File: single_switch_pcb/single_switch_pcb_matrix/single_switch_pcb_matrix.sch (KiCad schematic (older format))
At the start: 50 parts

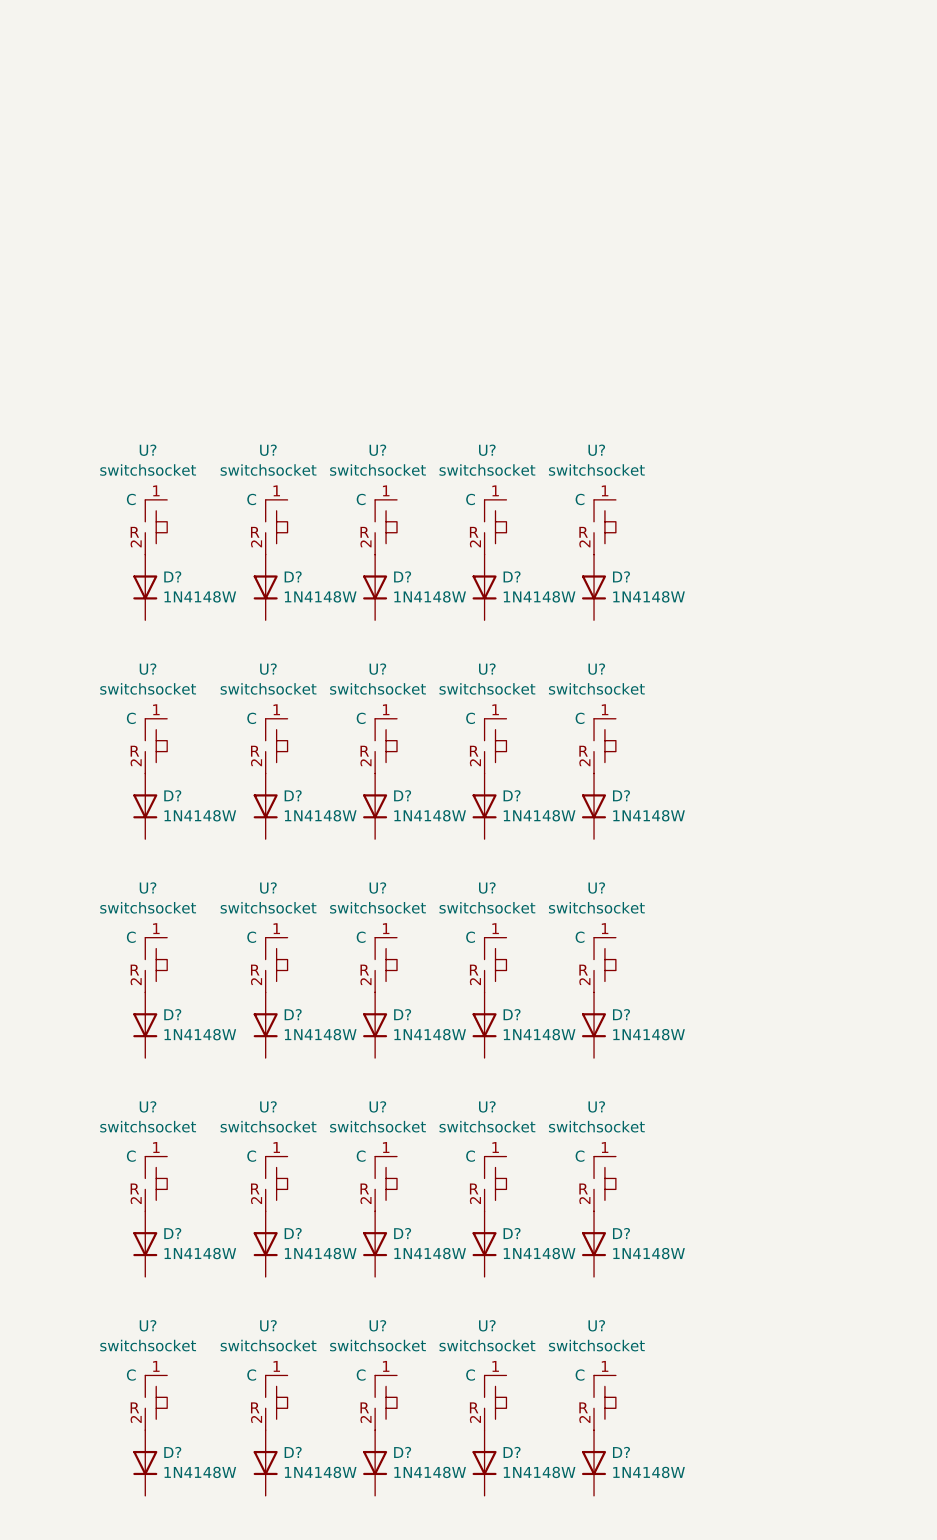
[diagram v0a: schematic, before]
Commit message: pcb matrix. done with column matrix. To do row matrix
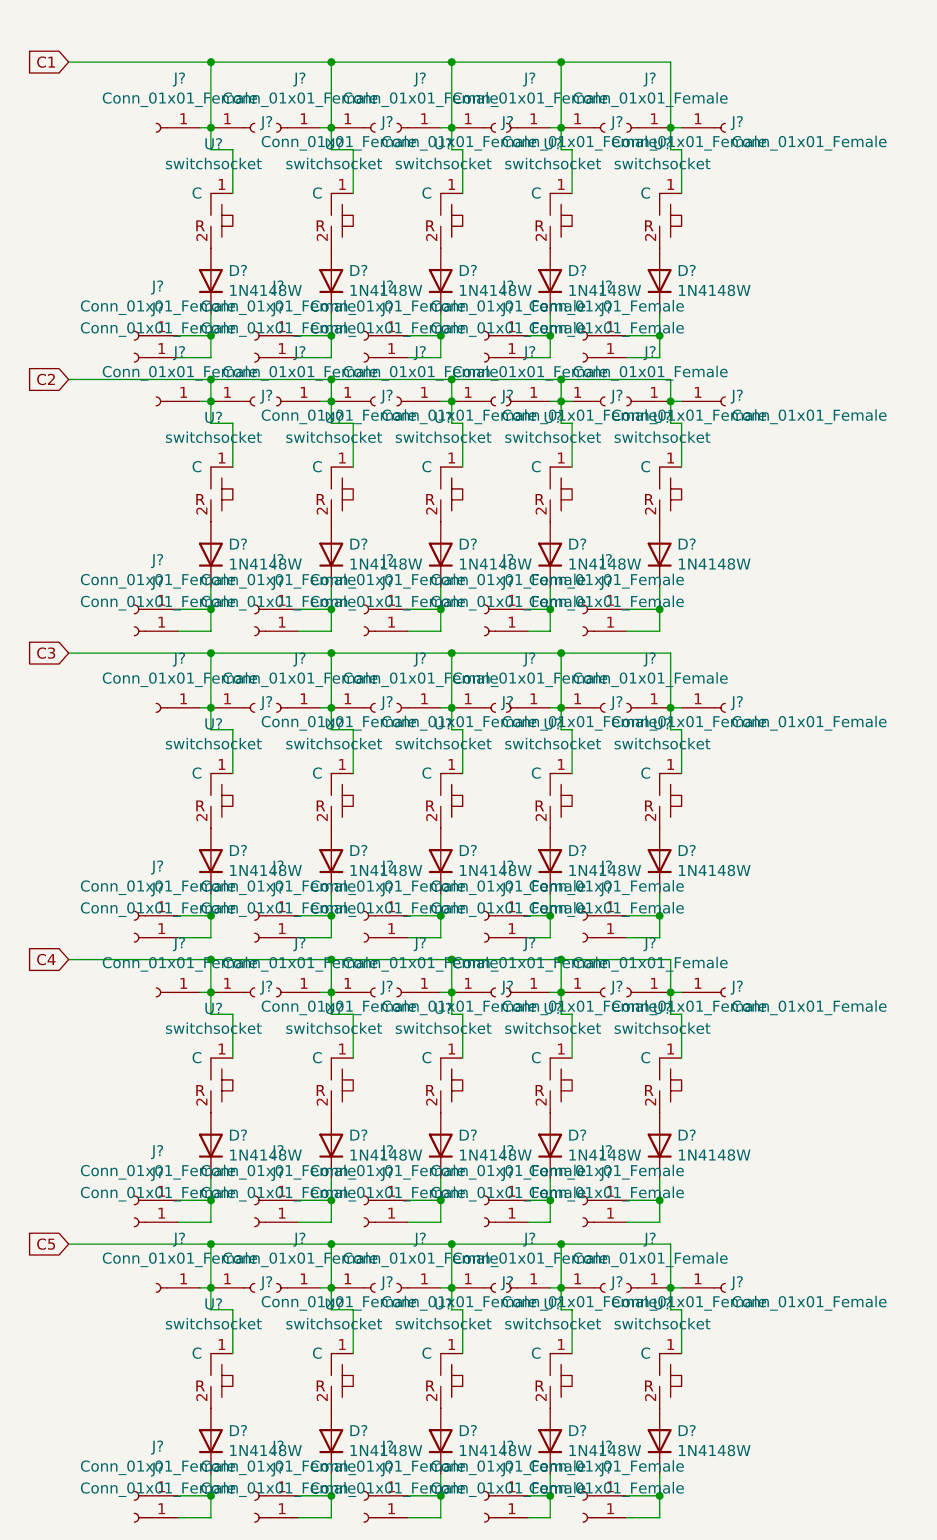
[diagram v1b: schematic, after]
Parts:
- removed D? (x20): 1N4148W, Diode_SMD:D_SOD-123, symbol Diode:1N4148W
- removed U? (x20): switchsocket, symbol hotswapsocket:switchsocket
- added D? (x20): 1N4148W, Diode_SMD:D_SOD-123, symbol Diode:1N4148W
- added J? (x100): Conn_01x01_Female, symbol Connector:Conn_01x01_Female
- added U? (x20): switchsocket, symbol hotswapsocket:switchsocket
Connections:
- net C1: now reaches U?.1 (C)
- net C1: now also U?.1 (C), U?.1 (C), U?.1 (C), U?.1 (C), J?.1 (Pin_1), J?.1 (Pin_1), J?.1 (Pin_1), J?.1 (Pin_1), J?.1 (Pin_1), J?.1 (Pin_1), J?.1 (Pin_1), J?.1 (Pin_1), J?.1 (Pin_1), J?.1 (Pin_1)
- net at D?.1 (K): now also J?.1 (Pin_1), J?.1 (Pin_1) (x5)
- new net: D?.2 (A), U?.2 (x20)
- new net: D?.1 (K), J?.1 (Pin_1), J?.1 (Pin_1) (x20)
- new net C2: J?.1 (Pin_1), J?.1 (Pin_1), J?.1 (Pin_1), J?.1 (Pin_1), J?.1 (Pin_1), J?.1 (Pin_1), J?.1 (Pin_1), J?.1 (Pin_1), J?.1 (Pin_1), J?.1 (Pin_1), U?.1 (C), U?.1 (C), U?.1 (C), U?.1 (C), U?.1 (C)
- new net C3: J?.1 (Pin_1), J?.1 (Pin_1), J?.1 (Pin_1), J?.1 (Pin_1), J?.1 (Pin_1), J?.1 (Pin_1), J?.1 (Pin_1), J?.1 (Pin_1), J?.1 (Pin_1), J?.1 (Pin_1), U?.1 (C), U?.1 (C), U?.1 (C), U?.1 (C), U?.1 (C)
- new net C4: J?.1 (Pin_1), J?.1 (Pin_1), J?.1 (Pin_1), J?.1 (Pin_1), J?.1 (Pin_1), J?.1 (Pin_1), J?.1 (Pin_1), J?.1 (Pin_1), J?.1 (Pin_1), J?.1 (Pin_1), U?.1 (C), U?.1 (C), U?.1 (C), U?.1 (C), U?.1 (C)
- new net C5: J?.1 (Pin_1), J?.1 (Pin_1), J?.1 (Pin_1), J?.1 (Pin_1), J?.1 (Pin_1), J?.1 (Pin_1), J?.1 (Pin_1), J?.1 (Pin_1), J?.1 (Pin_1), J?.1 (Pin_1), U?.1 (C), U?.1 (C), U?.1 (C), U?.1 (C), U?.1 (C)
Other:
- moved on the sheet: D?, U?

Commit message: done with row matrix. checked lines as well. move on to netlist
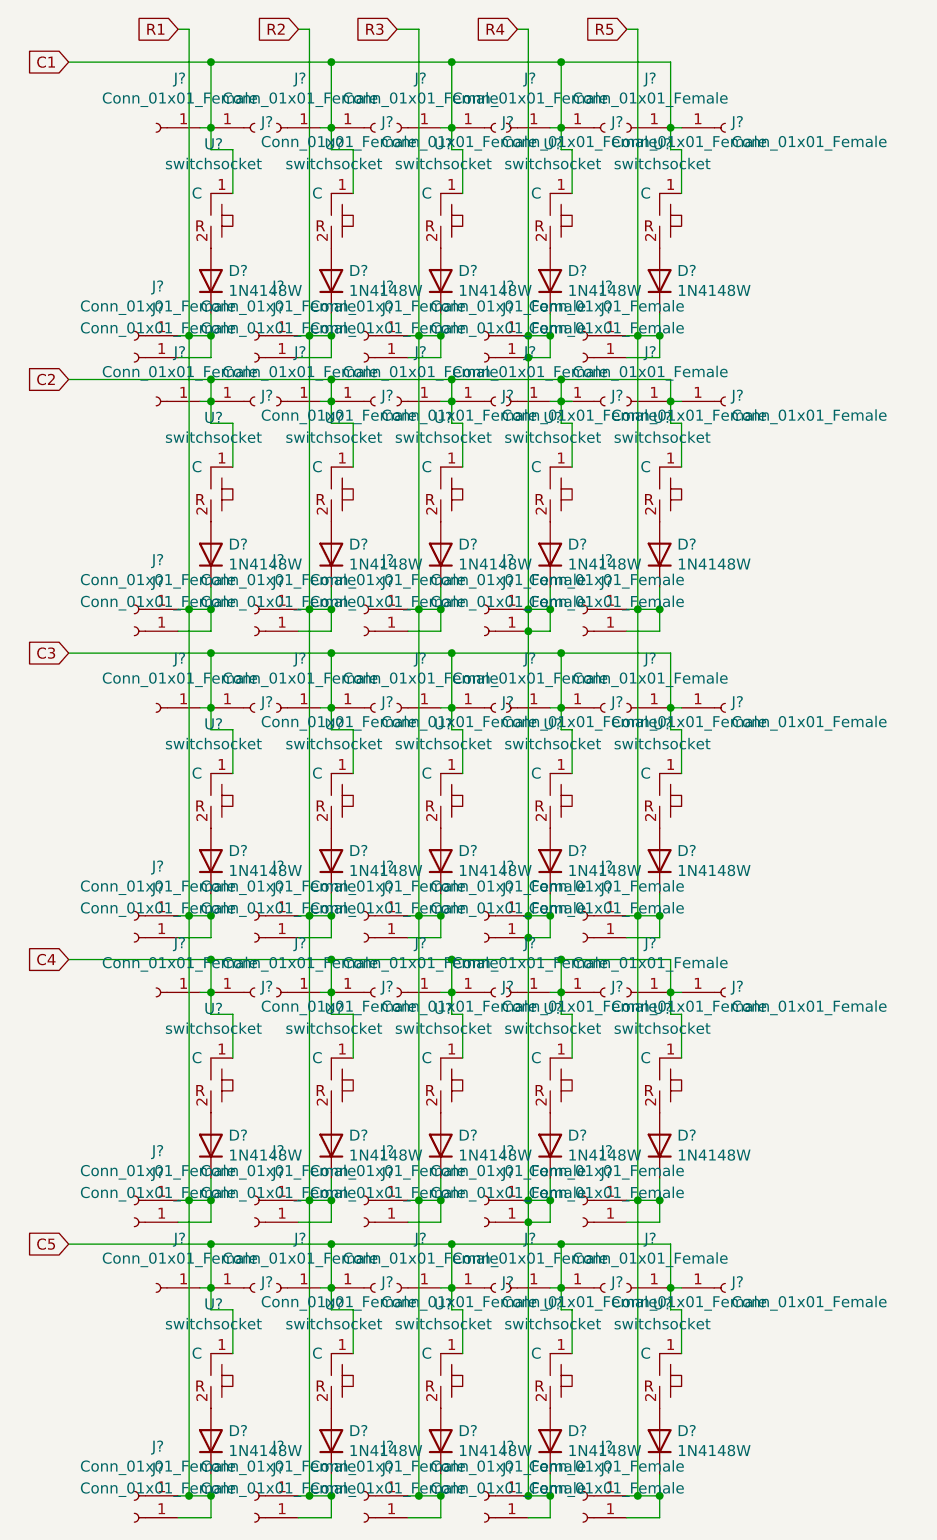
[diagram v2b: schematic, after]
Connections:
- net R1: now reaches D?.1 (K), J?.1 (Pin_1), J?.1 (Pin_1)
- net R1: now also D?.1 (K), D?.1 (K), D?.1 (K), D?.1 (K), J?.1 (Pin_1), J?.1 (Pin_1), J?.1 (Pin_1), J?.1 (Pin_1), J?.1 (Pin_1), J?.1 (Pin_1), J?.1 (Pin_1), J?.1 (Pin_1)
- net R2: now reaches D?.1 (K), J?.1 (Pin_1), J?.1 (Pin_1)
- net R2: now also D?.1 (K), D?.1 (K), D?.1 (K), D?.1 (K), J?.1 (Pin_1), J?.1 (Pin_1), J?.1 (Pin_1), J?.1 (Pin_1), J?.1 (Pin_1), J?.1 (Pin_1), J?.1 (Pin_1), J?.1 (Pin_1)
- net R3: now reaches D?.1 (K), J?.1 (Pin_1), J?.1 (Pin_1)
- net R3: now also D?.1 (K), D?.1 (K), D?.1 (K), D?.1 (K), J?.1 (Pin_1), J?.1 (Pin_1), J?.1 (Pin_1), J?.1 (Pin_1), J?.1 (Pin_1), J?.1 (Pin_1), J?.1 (Pin_1), J?.1 (Pin_1)
- net R4: now reaches D?.1 (K), J?.1 (Pin_1), J?.1 (Pin_1)
- net R4: now also D?.1 (K), D?.1 (K), D?.1 (K), D?.1 (K), J?.1 (Pin_1), J?.1 (Pin_1), J?.1 (Pin_1), J?.1 (Pin_1), J?.1 (Pin_1), J?.1 (Pin_1), J?.1 (Pin_1), J?.1 (Pin_1)
- net R5: now reaches D?.1 (K), J?.1 (Pin_1), J?.1 (Pin_1)
- net R5: now also D?.1 (K), D?.1 (K), D?.1 (K), D?.1 (K), J?.1 (Pin_1), J?.1 (Pin_1), J?.1 (Pin_1), J?.1 (Pin_1), J?.1 (Pin_1), J?.1 (Pin_1), J?.1 (Pin_1), J?.1 (Pin_1)
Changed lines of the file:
@@
 	4250 1900 4250 2000
 Wire Wire Line
-	4250 2000 4100 2000
+	4250 2000 4150 2000
 Wire Wire Line
 	4100 2100 4250 2100
@@
 Connection ~ 4250 2000
 Wire Wire Line
-	4650 2000 4800 2000
+	4650 2000 4700 2000
 Wire Wire Line
 	4800 2000 4800 1900
@@
 Connection ~ 4800 2000
 Wire Wire Line
-	5150 2000 5300 2000
+	5150 2000 5200 2000
 Wire Wire Line
 	5300 2000 5300 1900
@@
 Connection ~ 5800 2000
 Wire Wire Line
-	6150 2000 6300 2000
+	6150 2000 6200 2000
 Wire Wire Line
 	6300 2000 6300 1900
@@
 	4250 3150 4250 3250
 Wire Wire Line
-	4250 3250 4100 3250
+	4250 3250 4150 3250
 Wire Wire Line
 	4100 3350 4250 3350
@@
 Connection ~ 4250 3250
 Wire Wire Line
-	4650 3250 4800 3250
+	4650 3250 4700 3250
 Wire Wire Line
 	4800 3250 4800 3150
@@
 Connection ~ 4800 3250
 Wire Wire Line
-	5150 3250 5300 3250
+	5150 3250 5200 3250
 Wire Wire Line
 	5300 3250 5300 3150
@@
 Connection ~ 5800 3250
 Wire Wire Line
-	6150 3250 6300 3250
+	6150 3250 6200 3250
 Wire Wire Line
 	6300 3250 6300 3150
@@
 	4250 4550 4250 4650
 Wire Wire Line
-	4250 4650 4100 4650
-Wire Wire Line
 	4100 4750 4250 4750
 Wire Wire Line
@@
 Connection ~ 4250 4650
 Wire Wire Line
-	4650 4650 4800 4650
+	4650 4650 4700 4650
 Wire Wire Line
 	4800 4650 4800 4550
@@
 Connection ~ 4800 4650
 Wire Wire Line
-	5150 4650 5300 4650
+	5150 4650 5200 4650
 Wire Wire Line
 	5300 4650 5300 4550
@@
 Connection ~ 5800 4650
 Wire Wire Line
-	6150 4650 6300 4650
+	6150 4650 6200 4650
 Wire Wire Line
 	6300 4650 6300 4550
@@
 	4250 5850 4250 5950
 Wire Wire Line
-	4250 5950 4100 5950
+	4250 5950 4150 5950
 Wire Wire Line
 	4100 6050 4250 6050
@@
 Connection ~ 4250 5950
 Wire Wire Line
-	4650 5950 4800 5950
+	4650 5950 4700 5950
 Wire Wire Line
 	4800 5950 4800 5850
@@
 Connection ~ 4800 5950
 Wire Wire Line
-	5150 5950 5300 5950
+	5150 5950 5200 5950
 Wire Wire Line
 	5300 5950 5300 5850
@@
 Connection ~ 5800 5950
 Wire Wire Line
-	6150 5950 6300 5950
+	6150 5950 6200 5950
 Wire Wire Line
 	6300 5950 6300 5850
@@
 	4250 7200 4250 7300
 Wire Wire Line
-	4250 7300 4100 7300
-Wire Wire Line
 	4100 7400 4250 7400
 Wire Wire Line
@@
 Connection ~ 4250 7300
 Wire Wire Line
-	4650 7300 4800 7300
+	4650 7300 4700 7300
 Wire Wire Line
 	4800 7300 4800 7200
@@
 Connection ~ 4800 7300
 Wire Wire Line
-	5150 7300 5300 7300
+	5150 7300 5200 7300
 Wire Wire Line
 	5300 7300 5300 7200
@@
 Connection ~ 5800 7300
 Wire Wire Line
-	6150 7300 6300 7300
+	6150 7300 6200 7300
 Wire Wire Line
 	6300 7300 6300 7200
-Wire Wire Line
-	6150 7400 6300 7400
 Wire Wire Line
 	6300 7400 6300 7300
@@
 Wire Wire Line
 	4250 6150 4800 6150
+Text GLabel 4100 600  0    50   Input ~ 0
+R1
+Text GLabel 4650 600  0    50   Input ~ 0
+R2
+Text GLabel 5100 600  0    50   Input ~ 0
+R3
+Text GLabel 5650 600  0    50   Input ~ 0
+R4
+Text GLabel 6150 600  0    50   Input ~ 0
+R5
+Wire Wire Line
+	4250 7300 4150 7300
+Wire Wire Line
+	4100 600  4150 600
+Connection ~ 4150 7300
+Wire Wire Line
+	4150 7300 4100 7300
+Connection ~ 4150 5950
+Wire Wire Line
+	4150 5950 4100 5950
+Wire Wire Line
+	4150 5950 4150 7300
+Wire Wire Line
+	4150 600  4150 2000
+Wire Wire Line
+	4250 4650 4150 4650
+Connection ~ 4150 4650
+Wire Wire Line
+	4150 4650 4150 5950
+Wire Wire Line
+	4150 4650 4100 4650
+Connection ~ 4150 3250
+Wire Wire Line
+	4150 3250 4100 3250
+Wire Wire Line
+	4150 3250 4150 4650
+Connection ~ 4150 2000
+Wire Wire Line
+	4150 2000 4100 2000
+Wire Wire Line
+	4150 2000 4150 3250
+Wire Wire Line
+	4650 600  4700 600
+Wire Wire Line
+	4700 600  4700 2000
+Connection ~ 4700 7300
+Wire Wire Line
+	4700 7300 4800 7300
+Wire Wire Line
+	4800 5950 4700 5950
+Connection ~ 4700 5950
+Wire Wire Line
+	4700 5950 4700 7300
+Wire Wire Line
+	4800 4650 4700 4650
+Connection ~ 4700 4650
+Wire Wire Line
+	4700 4650 4700 5950
+Wire Wire Line
+	4800 3250 4700 3250
+Connection ~ 4700 3250
+Wire Wire Line
+	4700 3250 4700 4650
+Wire Wire Line
+	4800 2000 4700 2000
+Connection ~ 4700 2000
+Wire Wire Line
+	4700 2000 4700 3250
+Wire Wire Line
+	5100 600  5200 600
+Wire Wire Line
+	5200 600  5200 2000
+Connection ~ 5200 7300
+Wire Wire Line
+	5200 7300 5300 7300
+Wire Wire Line
+	5300 5950 5200 5950
+Connection ~ 5200 5950
+Wire Wire Line
+	5200 5950 5200 7300
+Wire Wire Line
+	5300 4650 5200 4650
+Connection ~ 5200 4650
+Wire Wire Line
+	5200 4650 5200 5950
+Wire Wire Line
+	5300 3250 5200 3250
+Connection ~ 5200 3250
+Wire Wire Line
+	5200 3250 5200 4650
+Wire Wire Line
+	5300 2000 5200 2000
+Connection ~ 5200 2000
+Wire Wire Line
+	5200 2000 5200 3250
+Wire Wire Line
+	5700 600  5700 2000
+Connection ~ 5700 7300
+Connection ~ 5700 2000
+Wire Wire Line
+	5700 2000 5700 2100
+Connection ~ 5700 2100
+Wire Wire Line
+	5700 2100 5700 3250
+Connection ~ 5700 3250
+Wire Wire Line
+	5700 3250 5700 3350
+Connection ~ 5700 3350
+Wire Wire Line
+	5700 3350 5700 4650
+Connection ~ 5700 4650
+Wire Wire Line
+	5700 4650 5700 4750
+Connection ~ 5700 4750
+Wire Wire Line
+	5700 4750 5700 5950
+Connection ~ 5700 5950
+Wire Wire Line
+	5700 5950 5700 6050
+Connection ~ 5700 6050
+Wire Wire Line
+	5700 6050 5700 7300
+Wire Wire Line
+	6150 7400 6300 7400
+Wire Wire Line
+	6200 600  6200 2000
+Connection ~ 6200 7300
+Wire Wire Line
+	6200 7300 6300 7300
+Wire Wire Line
+	6300 5950 6200 5950
+Connection ~ 6200 5950
+Wire Wire Line
+	6200 5950 6200 7300
+Wire Wire Line
+	6300 4650 6200 4650
+Connection ~ 6200 4650
+Wire Wire Line
+	6200 4650 6200 5950
+Wire Wire Line
+	6300 3250 6200 3250
+Connection ~ 6200 3250
+Wire Wire Line
+	6200 3250 6200 4650
+Wire Wire Line
+	6300 2000 6200 2000
+Connection ~ 6200 2000
+Wire Wire Line
+	6200 2000 6200 3250
+Wire Wire Line
+	5650 600  5700 600
+Wire Wire Line
+	6150 600  6200 600
 $EndSCHEMATC

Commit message: done with netlist. assigned footprints as well. move on to pcb desigh
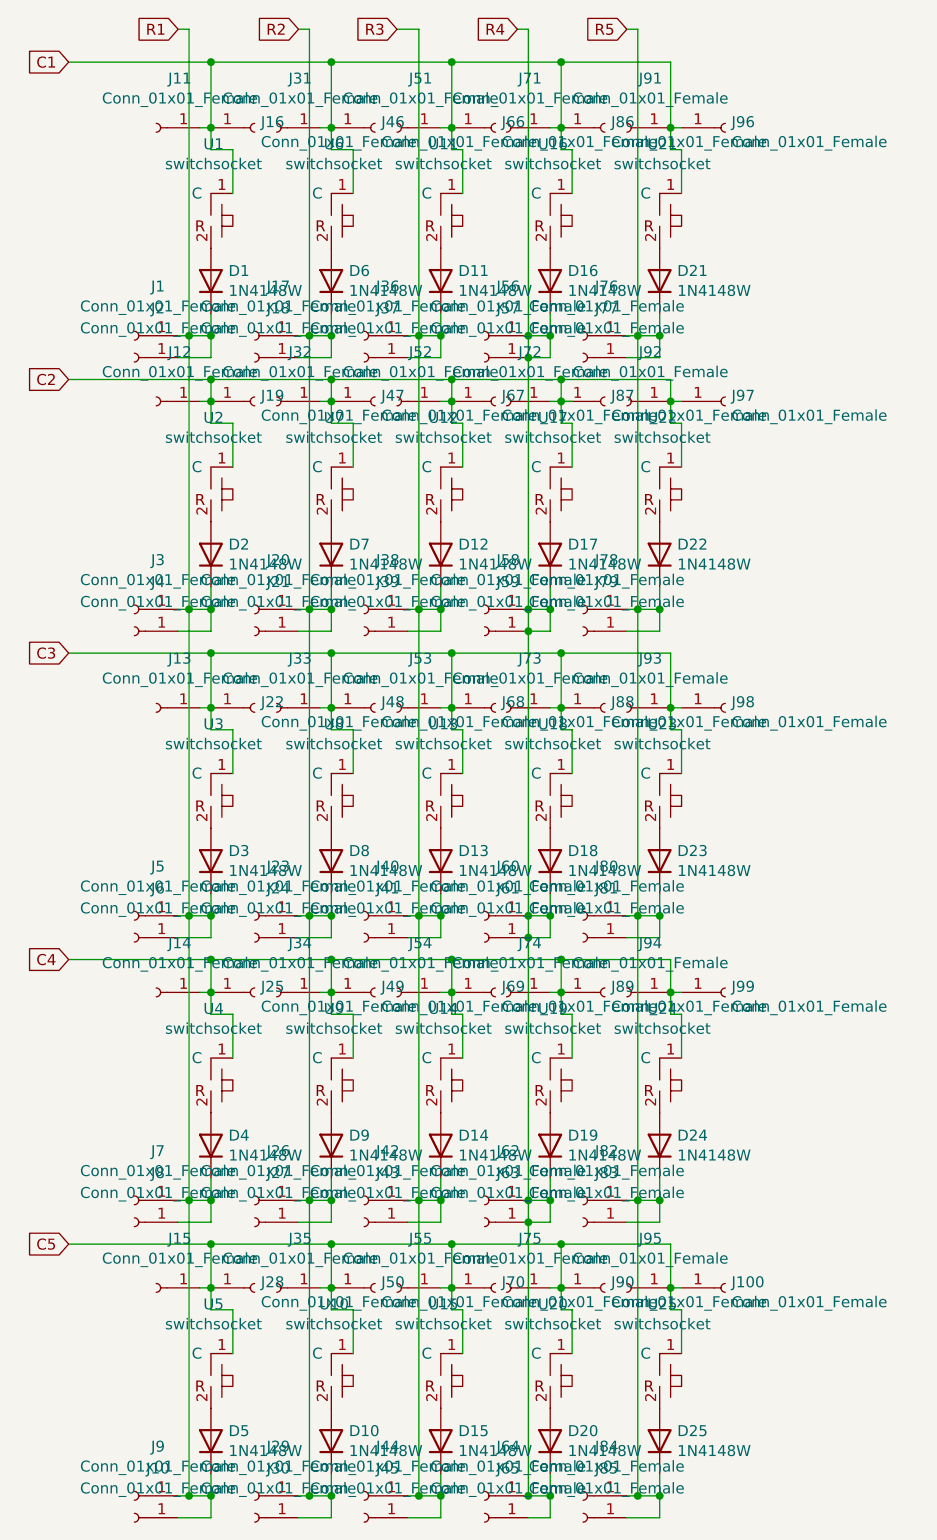
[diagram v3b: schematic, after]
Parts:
- J1, J10, J100, J11, J12, J13, J14, J15, J16, J17, J18, J19, J2, J20, J21, J22, J23, J24, J25, J26, J27, J28, J29, J3, J30, J31, J32, J33, J34, J35, J36, J37, J38, J39, J4, J40, J41, J42, J43, J44, J45, J46, J47, J48, J49, J5, J50, J51, J52, J53, J54, J55, J56, J57, J58, J59, J6, J60, J61, J62, J63, J64, J65, J66, J67, J68, J69, J7, J70, J71, J72, J73, J74, J75, J76, J77, J78, J79, J8, J80, J81, J82, J83, J84, J85, J86, J87, J88, J89, J9, J90, J91, J92, J93, J94, J95, J96, J97, J98, J99: renamed from J?; footprint (none) -> Connector_PinHeader_2.54mm:PinHeader_1x01_P2.54mm_Vertical
- U1, U10, U11, U12, U13, U14, U15, U16, U17, U18, U19, U2, U20, U21, U22, U23, U24, U25, U3, U4, U5, U6, U7, U8, U9: renamed from U?; footprint (none) -> hotswapsocket:hotswap socket
- gave numbers to parts that had none: 25
